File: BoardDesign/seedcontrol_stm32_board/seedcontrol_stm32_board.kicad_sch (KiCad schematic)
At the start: 37 parts, among them J1 Input, U2 MP1584EN, U3 STM32F401RCTx

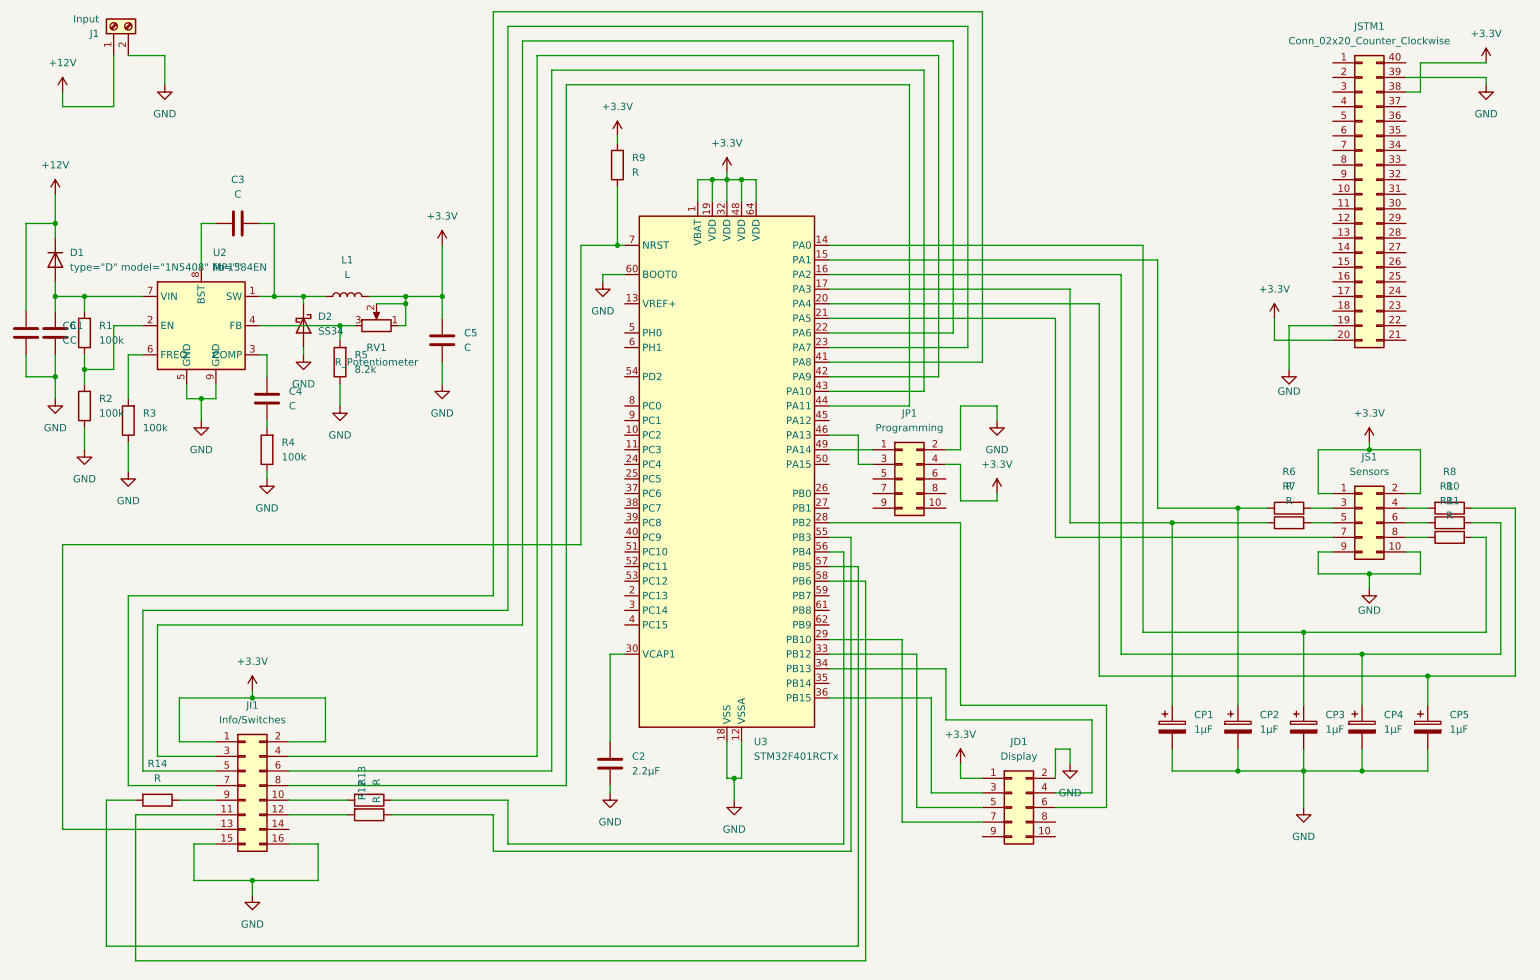
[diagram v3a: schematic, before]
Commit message: Finalized schematics. Placed all components in Boardview.
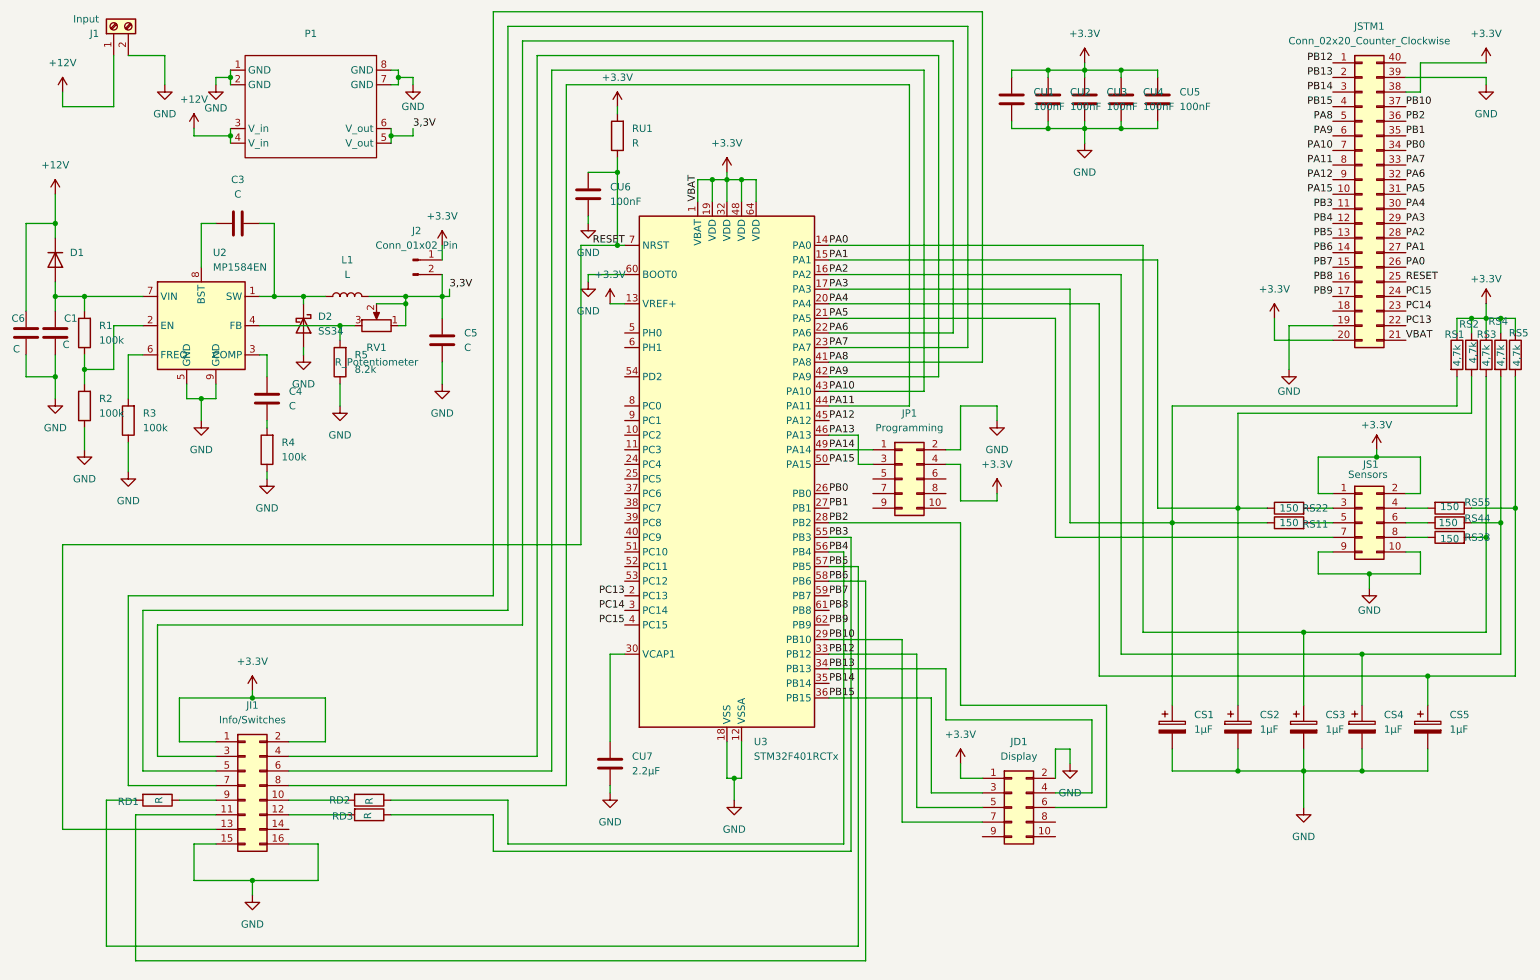
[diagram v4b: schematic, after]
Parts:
- added CU1, CU2, CU3, CU4, CU5, CU6: 100nF, Capacitor_SMD:C_0402_1005Metric, symbol Device:C
- added J2: Conn_01x02_Pin, Connector_PinHeader_2.54mm:PinHeader_1x02_P2.54mm_Vertical, symbol Connector:Conn_01x02_Pin
- added P1: ~, custom:Voltage_converter, symbol custom:Voltage_converter
- added RS1, RS2, RS3, RS4, RS5: 4,7k, Resistor_THT:R_Axial_DIN0309_L9.0mm_D3.2mm_P12.70mm_Horizontal, symbol Device:R
- RS11: renamed from R7; value R -> 150
- RS22: renamed from R6; value R -> 150
- RS33: renamed from R11; value R -> 150
- RS44: renamed from R10; value R -> 150
- RS55: renamed from R8; value R -> 150
- renumbered CP1 to CS1, CP2 to CS2, CP3 to CS3, CP4 to CS4, CP5 to CS5, C2 to CU7, R14 to RD1, R13 to RD2, R12 to RD3, R9 to RU1
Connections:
- net +12V: now also P1.3 (V_in), P1.4 (V_in)
- net +3.3V: now also JSTM1.21 (Pin_21), U3.13 (VREF+), CU1.2, CU2.2, CU3.2, CU4.2, CU5.2, J2.1 (Pin_1), RS1.1, RS2.1, RS3.1, RS4.1, RS5.1; no longer C5.2, L1.2, RV1.1, RV1.2
- net GND: now also CU1.1, CU2.1, CU3.1, CU4.1, CU5.1, CU6.1, P1.1 (GND), P1.2 (GND), P1.7 (GND), P1.8 (GND)
- net PA0: now reaches CS3.1, RS33.2, U3.14 (PA0)
- net PA0: now also JSTM1.26 (Pin_26), RS3.2
- net PA1: now reaches CS2.1, RS22.1, U3.15 (PA1)
- net PA1: now also JSTM1.27 (Pin_27), RS2.2
- net PA2: now reaches CS4.1, RS44.2, U3.16 (PA2)
- net PA2: now also JSTM1.28 (Pin_28), RS4.2
- net PA3: now reaches CS1.1, RS11.1, U3.17 (PA3)
- net PA3: now also JSTM1.29 (Pin_29), RS1.2
- net PC13: now reaches U3.2 (PC13)
- net PC13: now also JSTM1.22 (Pin_22)
- net PA4: now reaches CS5.1, RS55.1, U3.20 (PA4)
- net PA4: now also JSTM1.30 (Pin_30), RS5.2
- net PA5: now reaches JS1.7 (Pin_7), U3.21 (PA5)
- net PA5: now also JSTM1.31 (Pin_31)
- net PA6: now reaches JI1.3 (Pin_3), U3.22 (PA6)
- net PA6: now also JSTM1.32 (Pin_32)
- net PA7: now reaches JI1.5 (Pin_5), U3.23 (PA7)
- net PA7: now also JSTM1.33 (Pin_33)
- net PB0: now reaches U3.26 (PB0)
- net PB0: now also JSTM1.34 (Pin_34)
- net PB1: now reaches U3.27 (PB1)
- net PB1: now also JSTM1.35 (Pin_35)
- net PB2: now reaches JD1.6 (Pin_6), U3.28 (PB2)
- net PB2: now also JSTM1.36 (Pin_36)
- net PB10: now reaches JD1.7 (Pin_7), U3.29 (PB10)
- net PB10: now also JSTM1.37 (Pin_37)
- net PC14: now reaches U3.3 (PC14)
- net PC14: now also JSTM1.23 (Pin_23)
- net PB12: now reaches JD1.5 (Pin_5), U3.33 (PB12)
- net PB12: now also JSTM1.1 (Pin_1)
- net PB13: now reaches JD1.4 (Pin_4), U3.34 (PB13)
- net PB13: now also JSTM1.2 (Pin_2)
- net PB14: now reaches U3.35 (PB14)
- net PB14: now also JSTM1.3 (Pin_3)
- net PB15: now reaches JD1.3 (Pin_3), U3.36 (PB15)
- net PB15: now also JSTM1.4 (Pin_4)
- net PC15: now reaches U3.4 (PC15)
- net PC15: now also JSTM1.24 (Pin_24)
- net PA8: now reaches JI1.7 (Pin_7), U3.41 (PA8)
- net PA8: now also JSTM1.5 (Pin_5)
- net PA9: now reaches JI1.4 (Pin_4), U3.42 (PA9)
- net PA9: now also JSTM1.6 (Pin_6)
- net PA10: now reaches JI1.6 (Pin_6), U3.43 (PA10)
- net PA10: now also JSTM1.7 (Pin_7)
- net PA11: now reaches JI1.8 (Pin_8), U3.44 (PA11)
- net PA11: now also JSTM1.8 (Pin_8)
- net PA12: now reaches U3.45 (PA12)
- net PA12: now also JSTM1.9 (Pin_9)
- net PA13: now reaches JP1.3 (Pin_3), U3.46 (PA13)
- net PA14: now reaches JP1.1 (Pin_1), U3.49 (PA14)
- net PA15: now reaches U3.50 (PA15)
- net PA15: now also JSTM1.10 (Pin_10)
- net PB3: now reaches RD3.1, U3.55 (PB3)
- net PB3: now also JSTM1.11 (Pin_11)
- net PB4: now reaches RD2.1, U3.56 (PB4)
- net PB4: now also JSTM1.12 (Pin_12)
- net PB5: now reaches RD1.2, U3.57 (PB5)
- net PB5: now also JSTM1.13 (Pin_13)
- net PB6: now reaches JI1.11 (Pin_11), U3.58 (PB6)
- net PB6: now also JSTM1.14 (Pin_14)
- net PB7: now reaches U3.59 (PB7)
- net PB7: now also JSTM1.15 (Pin_15)
- net PB8: now reaches U3.61 (PB8)
- net PB8: now also JSTM1.16 (Pin_16)
- net PB9: now reaches U3.62 (PB9)
- net PB9: now also JSTM1.17 (Pin_17)
- net RESET: now reaches JI1.13 (Pin_13), RU1.1, U3.7 (NRST)
- net RESET: now also JSTM1.25 (Pin_25), CU6.2
- new net 3,3V: C5.2, J2.2 (Pin_2), L1.2, P1.5 (V_out), P1.6 (V_out), RV1.1, RV1.2
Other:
- moved on the sheet: RU1

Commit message: Final Board design.
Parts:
- D2: footprint Diode_SMD:D_SMC -> Diode_SMD:D_SMA
- RS1, RS2, RS3, RS4, RS5: value 4,7k -> 4,7-10k
- RV1: value R_Potentiometer -> R_Pot
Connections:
- net +12V: now also D1.1 (A); no longer C6.2, D1.2 (K), P1.3 (V_in), P1.4 (V_in)
- net V12: now reaches C1.2, R1.2, U2.7 (VIN)
- net V12: now also C6.2, D1.2 (K), P1.3 (V_in), P1.4 (V_in); no longer D1.1 (A)
- net 3,3V renamed V3,3
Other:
- moved on the sheet: D1, D2, JSTM1
